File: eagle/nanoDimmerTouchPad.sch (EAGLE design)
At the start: 12 parts

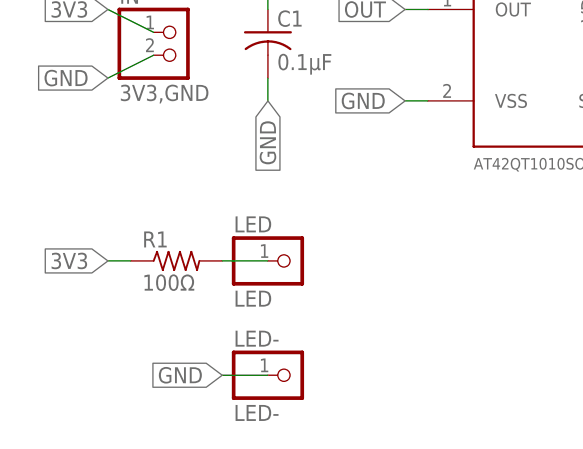
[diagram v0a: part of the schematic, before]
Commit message: change indicator LED resistor from 100 to 4700 ohm to match Legrand Adorne brightness
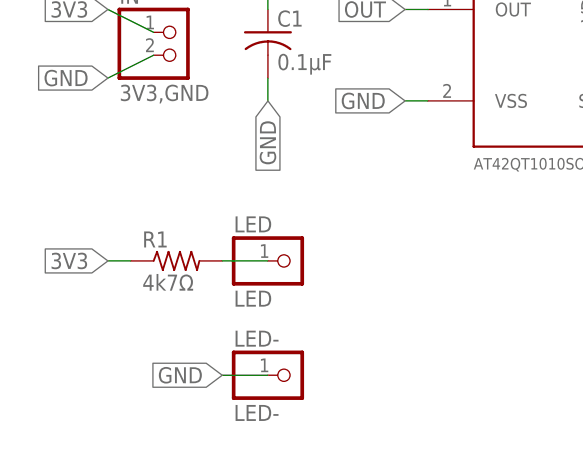
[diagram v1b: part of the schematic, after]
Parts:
- R1: value 100Ω -> 4k7Ω
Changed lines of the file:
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@@
 <part name="LED" library="pinhead" library_urn="urn:adsk.eagle:library:325" deviceset="PINHD-1X1" device="" package3d_urn="urn:adsk.eagle:package:22485/2" value="LED"/>
 <part name="LED-" library="pinhead" library_urn="urn:adsk.eagle:library:325" deviceset="PINHD-1X1" device="" package3d_urn="urn:adsk.eagle:package:22485/2" value="LED-"/>
-<part name="R1" library="rcl" library_urn="urn:adsk.eagle:library:334" deviceset="R-US_" device="0204/7" package3d_urn="urn:adsk.eagle:package:23498/2" value="100Ω"/>
+<part name="R1" library="rcl" library_urn="urn:adsk.eagle:library:334" deviceset="R-US_" device="0204/7" package3d_urn="urn:adsk.eagle:package:23498/2" value="4k7Ω"/>
 <part name="OPTO" library="optocoupler" library_urn="urn:adsk.eagle:library:320" deviceset="PC817" device="" package3d_urn="urn:adsk.eagle:package:21938/1"/>
 <part name="R3" library="rcl" library_urn="urn:adsk.eagle:library:334" deviceset="R-US_" device="0204/7" package3d_urn="urn:adsk.eagle:package:23498/2" value="100Ω"/>

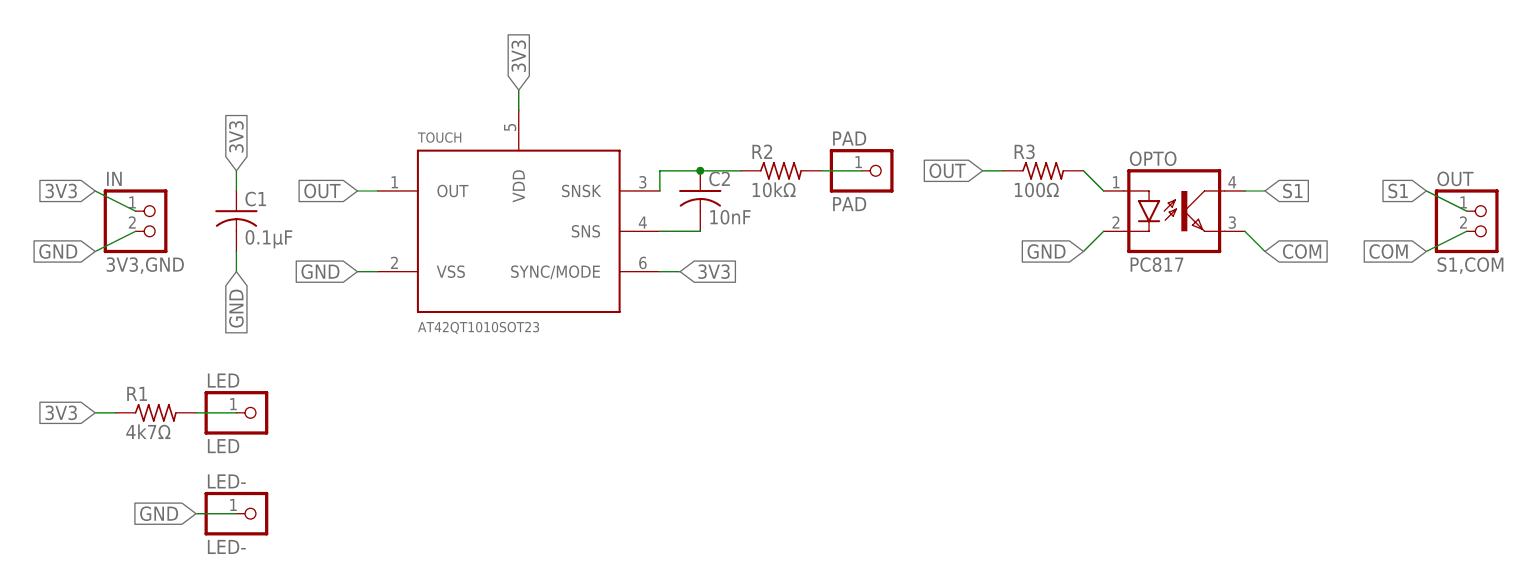
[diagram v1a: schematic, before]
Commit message: v1.0: paranoid isolation of sense circuits, no ground planes, SMD resistors and capacitors
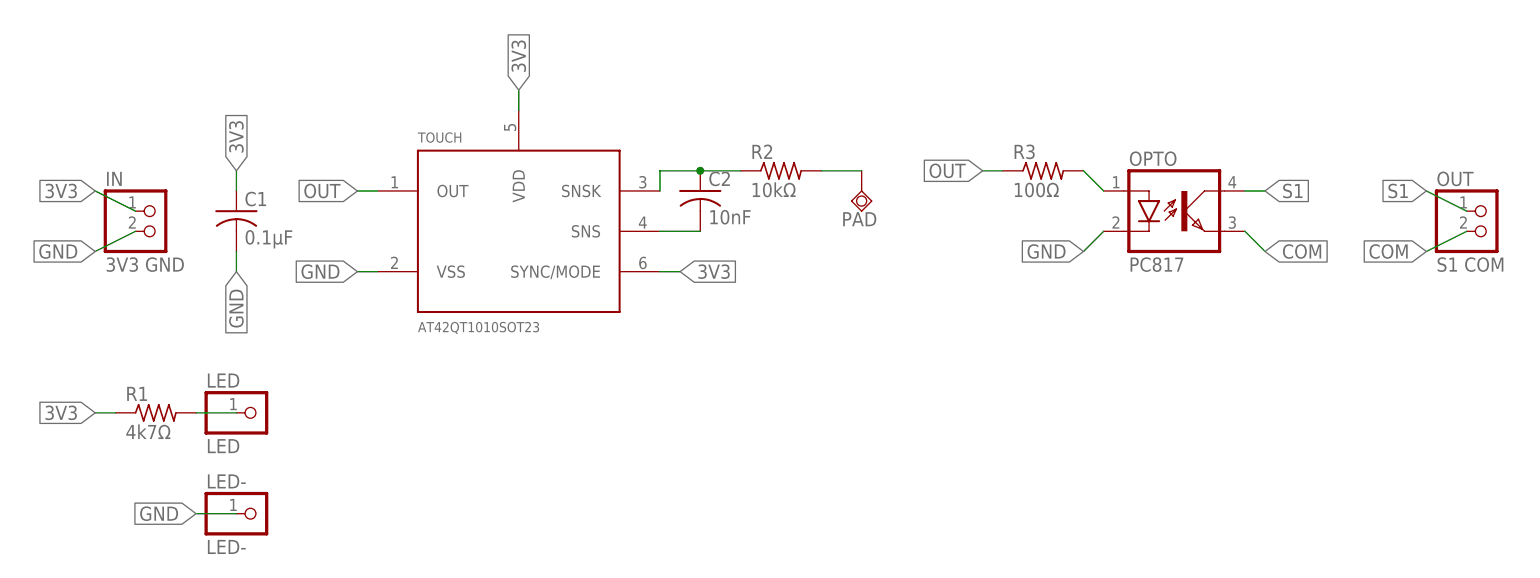
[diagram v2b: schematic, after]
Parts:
- C1, C2: device rcl:C-US025-024X044 -> rcl:C-USC1206
- IN: value 3V3,GND -> 3V3 GND
- OUT: value S1,COM -> S1 COM
- PAD: value PAD -> TPSQPAD1-13; device pinhead:PINHD-1X1 -> testpad:TPSQPAD1-13
- R1, R2, R3: device rcl:R-US_0204/7 -> rcl:R-US_R1206
- TOUCH: device SparkFun-Sensors:AT42QT1010SOT23 -> SparkFun-Retired:AT42QT1010SOT23
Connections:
- net PAD: now also PAD.TP; no longer PAD.1
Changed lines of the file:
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@@
 </classes>
 <parts>
-<part name="IN" library="pinhead" library_urn="urn:adsk.eagle:library:325" deviceset="PINHD-1X2" device="" package3d_urn="urn:adsk.eagle:package:22435/2" value="3V3,GND"/>
-<part name="OUT" library="pinhead" library_urn="urn:adsk.eagle:library:325" deviceset="PINHD-1X2" device="" package3d_urn="urn:adsk.eagle:package:22435/2" value="S1,COM"/>
-<part name="C1" library="rcl" library_urn="urn:adsk.eagle:library:334" deviceset="C-US" device="025-024X044" package3d_urn="urn:adsk.eagle:package:23630/1" value="0.1µF"/>
-<part name="TOUCH" library="SparkFun-Sensors" deviceset="AT42QT1010" device="SOT23"/>
-<part name="C2" library="rcl" library_urn="urn:adsk.eagle:library:334" deviceset="C-US" device="025-024X044" package3d_urn="urn:adsk.eagle:package:23630/1" value="10nF"/>
-<part name="R2" library="rcl" library_urn="urn:adsk.eagle:library:334" deviceset="R-US_" device="0204/7" package3d_urn="urn:adsk.eagle:package:23498/2" value="10kΩ"/>
-<part name="PAD" library="pinhead" library_urn="urn:adsk.eagle:library:325" deviceset="PINHD-1X1" device="" package3d_urn="urn:adsk.eagle:package:22485/2" value="PAD"/>
+<part name="IN" library="pinhead" library_urn="urn:adsk.eagle:library:325" deviceset="PINHD-1X2" device="" package3d_urn="urn:adsk.eagle:package:22435/2" value="3V3  GND"/>
+<part name="OUT" library="pinhead" library_urn="urn:adsk.eagle:library:325" deviceset="PINHD-1X2" device="" package3d_urn="urn:adsk.eagle:package:22435/2" value="S1  COM"/>
+<part name="C1" library="rcl" library_urn="urn:adsk.eagle:library:334" deviceset="C-US" device="C1206" package3d_urn="urn:adsk.eagle:package:23618/2" value="0.1µF"/>
+<part name="TOUCH" library="SparkFun-Retired" deviceset="AT42QT1010" device="SOT23"/>
+<part name="C2" library="rcl" library_urn="urn:adsk.eagle:library:334" deviceset="C-US" device="C1206" package3d_urn="urn:adsk.eagle:package:23618/2" value="10nF"/>
+<part name="R2" library="rcl" library_urn="urn:adsk.eagle:library:334" deviceset="R-US_" device="R1206" package3d_urn="urn:adsk.eagle:package:23540/2" value="10kΩ"/>
 <part name="LED" library="pinhead" library_urn="urn:adsk.eagle:library:325" deviceset="PINHD-1X1" device="" package3d_urn="urn:adsk.eagle:package:22485/2" value="LED"/>
 <part name="LED-" library="pinhead" library_urn="urn:adsk.eagle:library:325" deviceset="PINHD-1X1" device="" package3d_urn="urn:adsk.eagle:package:22485/2" value="LED-"/>
-<part name="R1" library="rcl" library_urn="urn:adsk.eagle:library:334" deviceset="R-US_" device="0204/7" package3d_urn="urn:adsk.eagle:package:23498/2" value="4k7Ω"/>
+<part name="R1" library="rcl" library_urn="urn:adsk.eagle:library:334" deviceset="R-US_" device="R1206" package3d_urn="urn:adsk.eagle:package:23540/2" value="4k7Ω"/>
 <part name="OPTO" library="optocoupler" library_urn="urn:adsk.eagle:library:320" deviceset="PC817" device="" package3d_urn="urn:adsk.eagle:package:21938/1"/>
-<part name="R3" library="rcl" library_urn="urn:adsk.eagle:library:334" deviceset="R-US_" device="0204/7" package3d_urn="urn:adsk.eagle:package:23498/2" value="100Ω"/>
+<part name="R3" library="rcl" library_urn="urn:adsk.eagle:library:334" deviceset="R-US_" device="R1206" package3d_urn="urn:adsk.eagle:package:23540/2" value="100Ω"/>
+<part name="PAD" library="testpad" library_urn="urn:adsk.eagle:library:385" deviceset="TPSQ" device="PAD1-13" package3d_urn="urn:adsk.eagle:package:27946/1"/>
 </parts>
 <sheets>
@@
 <attribute name="VALUE" x="72.39" y="65.278" size="1.778" layer="96"/>
 </instance>
-<instance part="PAD" gate="G$1" x="88.9" y="68.58" smashed="yes">
-<attribute name="NAME" x="82.55" y="71.755" size="1.778" layer="95"/>
-<attribute name="VALUE" x="82.55" y="63.5" size="1.778" layer="96"/>
-</instance>
 <instance part="LED" gate="G$1" x="10.16" y="38.1" smashed="yes">
 <attribute name="NAME" x="3.81" y="41.275" size="1.778" layer="95"/>
@@
 <attribute name="NAME" x="105.41" y="70.0786" size="1.778" layer="95"/>
 <attribute name="VALUE" x="105.41" y="65.278" size="1.778" layer="96"/>
+</instance>
+<instance part="PAD" gate="G$1" x="86.36" y="66.04" smashed="yes">
+<attribute name="NAME" x="83.82" y="61.595" size="1.778" layer="95"/>
+<attribute name="TP_SIGNAL_NAME" x="88.9" y="64.77" size="1.778" layer="97"/>
 </instance>
 </instances>
@@
 <pinref part="R2" gate="G$1" pin="2"/>
 <wire x1="81.28" y1="68.58" x2="86.36" y2="68.58" width="0.1524" layer="91"/>
-<pinref part="PAD" gate="G$1" pin="1"/>
+<pinref part="PAD" gate="G$1" pin="TP"/>
 </segment>
 </net>
